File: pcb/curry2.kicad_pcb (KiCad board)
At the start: 2 copper layers, 100.4 x 114.4 mm, 168 parts, among them CON101 AVR-ISP-6, IC101 ATMEGA88-A, K301 CONN_3, K302 CONN_3, K401 CONN_3, K402 CONN_3, K501 CONN_3, K502 CONN_3, K601 CONN_3, K602 CONN_3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

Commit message: almost done pre merger
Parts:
- C104, C105, C107, C108, C111, C112, C114, C115, R1: moved to B.Cu
- moved R1 106.6 mm to (95.1, 127.9), turned to 90 degrees
- moved C202 20.9 mm to (128.7, 133.7), turned to 270 degrees
- moved C113 5.95 mm to (116.7, 131.3), turned to 270 degrees
- moved C106 3.69 mm to (132.0, 123.4), turned to 0 degrees
- moved C108 3.05 mm to (174.0, 156.5)
- moved C111 2.03 mm to (176.5, 156.5)
- moved C125 1.20 mm to (112.1, 128.9)
- moved C206 1.02 mm to (106.8, 123.4)
- moved C112 0.90 mm to (157.5, 156.7), turned to 270 degrees
- moved C110 0.81 mm to (132.1, 126.7)
- moved C114 0.72 mm to (140.0, 156.5)
- turned C104 to 90 degrees
- turned C105 to 270 degrees
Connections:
- U101 pad 35: GND -> (no net)
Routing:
- net HVDD: track 69.3 -> 235.2 mm, vias 4 -> 9
- net HVSS: track 94.9 -> 260.8 mm, vias 4 -> 8
- net AVDD: track 59.6 -> 154.7 mm, vias 6 -> 8
- net AGND: track 174.6 -> 238.9 mm, vias 21 -> 49
- net GND: track 41.3 -> 97.5 mm, vias 17 -> 36
- net /HW: track 52.8 -> 81.1 mm, vias 2 -> 3
- net N-0000028: track 12.6 -> 40.5 mm, vias 0 -> 1
- net N-0000097: track 0.00 -> 20.3 mm
- net N-0000094: track 0.00 -> 18.3 mm, vias 0 -> 1
- net N-0000063: track 4.06 -> 9.40 mm
- net N-0000035: track 0.00 -> 5.23 mm
- net N-0000045: track 55.2 -> 59.8 mm
- net N-00000103: track 28.3 -> 24.1 mm
- net N-0000030: track 0.00 -> 3.66 mm
- net N-0000090: track 22.9 -> 20.1 mm
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
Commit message: pcb done just needs currentsensors
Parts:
- removed BT101: BATTERY, CR2032H
- removed X101: CRYSTAL, SIL-2
- added P1: CONN_4, PIN_ARRAY_4x1, F.Cu at (164.2, 106.9)
- added P2: CONN_4, PIN_ARRAY_4x1, F.Cu at (177.1, 110.0)
- R1: value R -> 0R?
- R102: value R -> 4k7
- R302, R305, R309, R402, R405, R409, R502, R505, R509, R602, R605, R609: value 0 -> 0R
- R307, R314, R407, R414, R507, R514, R607, R614: value 10 -> 10R
- moved C101 0.25 mm to (122.2, 114.4)
- turned R1 to 270 degrees
- turned R102 to 90 degrees
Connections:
- IC101 pad 10: (no net) -> N-0000066
- IC101 pad 11: N-0000059 -> (no net)
- IC101 pad 21: (no net) -> GND
- IC101 pad 5: (no net) -> GND
- P102 pad 2: N-0000059 -> N-0000066
- P102 pad 4: (no net) -> N-0000066
- P102 pad 6: (no net) -> N-0000066
- P102 pad 8: N-0000059 -> N-0000066
- P301 pad 2: (no net) -> AGND
- P301 pad 4: (no net) -> AGND
- P301 pad 6: (no net) -> AGND
- P301 pad 8: (no net) -> AGND
- P401 pad 2: (no net) -> AGND
- P401 pad 4: (no net) -> AGND
- P401 pad 6: (no net) -> AGND
- P401 pad 8: (no net) -> AGND
- P501 pad 2: (no net) -> AGND
- P501 pad 4: (no net) -> AGND
- P501 pad 6: (no net) -> AGND
- P501 pad 8: (no net) -> AGND
- P601 pad 2: (no net) -> AGND
- P601 pad 4: (no net) -> AGND
- P601 pad 6: (no net) -> AGND
- P601 pad 8: (no net) -> AGND
- R1 pad 1: AGND -> GND
- R1 pad 2: GND -> AGND
- R102 pad 1: DVDD -> /SCL
- R102 pad 2: /SCL -> DVDD
- U101 pad 10: DB4 -> DB3
- U101 pad 11: DB5 -> DB4
- U101 pad 12: DB6 -> DB5
- U101 pad 13: DB7 -> DB6
- U101 pad 15: DB8 -> DB7
- U101 pad 16: DB9 -> DB8
- U101 pad 18: DB10 -> DB9
- U101 pad 19: DB11 -> DB10
- U101 pad 21: DB12 -> DB11
- U101 pad 22: DB13 -> DB12
- U101 pad 24: DB15 -> DB13
- U101 pad 26: /RD -> DB15
- U101 pad 32: (no net) -> /RD
- U101 pad 9: DB3 -> GND
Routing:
- net N-0000059: track 34.2 -> 0.00 mm, vias 1 -> 0
- net N-0000066: track 0.00 -> 25.4 mm
- net +5V: track 62.0 -> 86.6 mm
- net /SDA: track 100.9 -> 118.8 mm
- net /RD: track 23.3 -> 40.0 mm, vias 0 -> 2
- net GND: track 97.5 -> 85.7 mm, vias 36 -> 28
- net /SCL: track 99.7 -> 108.4 mm, vias 1 -> 2
- net N-0000051: track 0.00 -> 7.93 mm
- net DB4: track 21.8 -> 17.3 mm
- net DB10: track 16.6 -> 12.0 mm
- net DB6: track 20.6 -> 16.2 mm
- net DB7: track 16.5 -> 13.6 mm
- net DB11: track 12.5 -> 10.1 mm
- net DB3: track 19.2 -> 21.4 mm
- net DB9: track 18.6 -> 16.4 mm
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
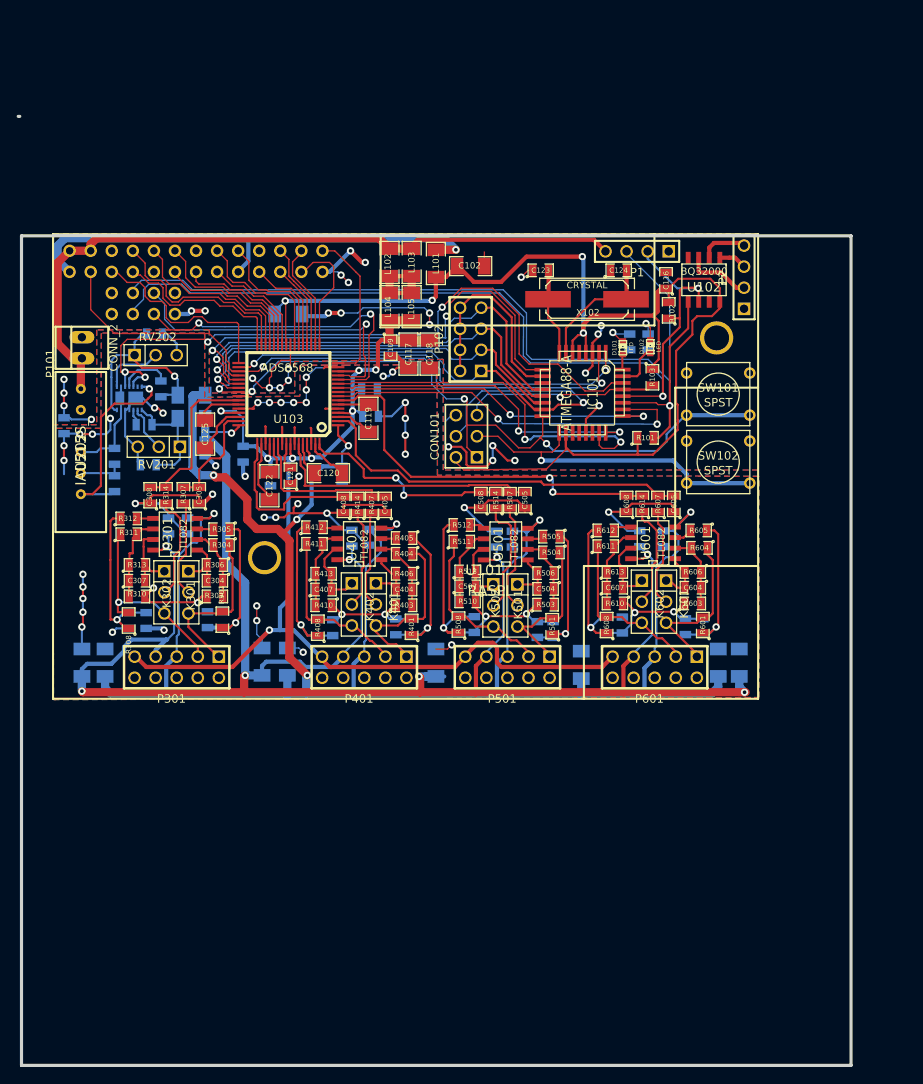
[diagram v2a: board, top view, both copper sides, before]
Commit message: added ina board
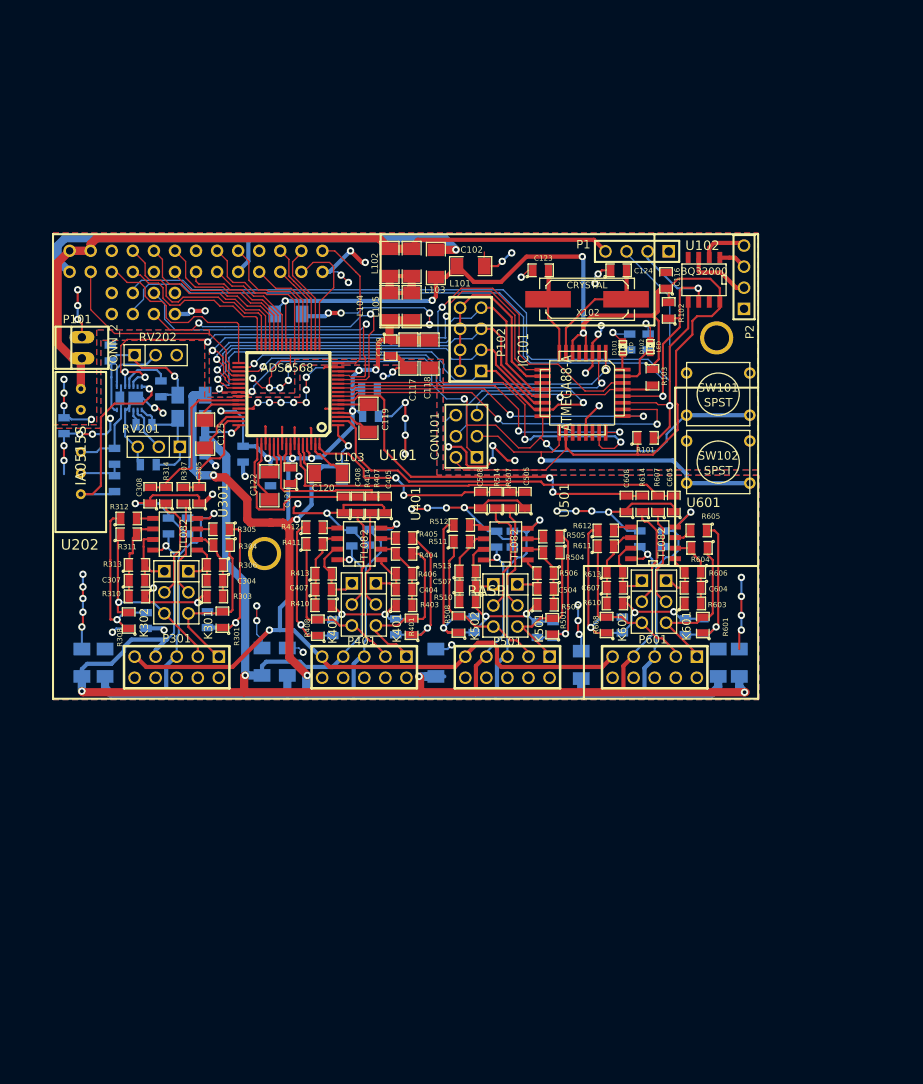
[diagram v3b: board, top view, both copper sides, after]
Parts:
- moved C204 5.80 mm to (100.7, 119.1), turned to 90 degrees
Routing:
- net AGND: track 238.9 -> 252.1 mm, vias 49 -> 57
- net GND: track 85.7 -> 98.6 mm, vias 28 -> 35
- net (no net): track 2.12 -> 8.87 mm, vias 1 -> 4
- net N-00000102: track 23.6 -> 20.2 mm
- net HVSS: track 260.8 -> 259.2 mm
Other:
- board outline removed
- rule pad_to_mask_clearance: 0.254 -> 0.001
- rule trace_min: 0.154 -> 0.16

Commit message: final release pre order
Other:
- board text added: "A"
- board text added: "B"
- board text added: "C"
- board text added: "D"
- board text added: "ETF"
- board text added: "Rasdaq"
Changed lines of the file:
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@@
     (links 432)
     (no_connects 0)
-    (area 75.945999 103.5409 180.4311 161.5996)
+    (area 93.308934 103.5409 180.4311 161.5996)
     (thickness 1.6002)
-    (drawings 0)
+    (drawings 6)
     (tracks 1983)
     (zones 0)
@@
     (19 F.Paste user hide)
     (20 B.SilkS user hide)
-    (21 F.SilkS user hide)
+    (21 F.SilkS user)
     (22 B.Mask user hide)
     (23 F.Mask user hide)
@@
   )
   (setup
-    (last_trace_width 0.508)
+    (last_trace_width 0.254)
     (user_trace_width 0.16)
     (user_trace_width 0.254)
@@
     )
   )
+  (gr_text ETF (at 138.684 128.778 90) (layer F.SilkS)
+    (effects (font (size 2.032 1.524) (thickness 0.3048)))
+  )
+  (gr_text D (at 173.99 155.448) (layer F.SilkS)
+    (effects (font (size 2.032 1.524) (thickness 0.3048)))
+  )
+  (gr_text C (at 155.956 155.575) (layer F.SilkS)
+    (effects (font (size 2.032 1.524) (thickness 0.3048)))
+  )
+  (gr_text B (at 138.938 155.321) (layer F.SilkS)
+    (effects (font (size 2.032 1.524) (thickness 0.3048)))
+  )
+  (gr_text A (at 116.332 155.448) (layer F.SilkS)
+    (effects (font (size 2.032 1.524) (thickness 0.3048)))
+  )
+  (gr_text "Rasdaq\n" (at 96.012 146.685 270) (layer F.SilkS)
+    (effects (font (size 3 2) (thickness 0.3048)))
+  )
   (segment (start 176.53 154.813) (end 176.53 152.781) (width 0.254) (layer Front) (net 0))
